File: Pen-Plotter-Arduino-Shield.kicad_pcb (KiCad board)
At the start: 2 copper layers, 68.6 x 53.3 mm, 41 parts, among them J1 CONN_08LOCK, J10 CONN_08LOCK, J11 CONN_04LOCK, J12 CONN_03LOCK, J13 691137710002, J14 CONN_03LOCK, J15 CONN_03LOCK, J16 CONN_03LOCK, J17 CONN_03LOCK, J18 CONN_03X2FEMALE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

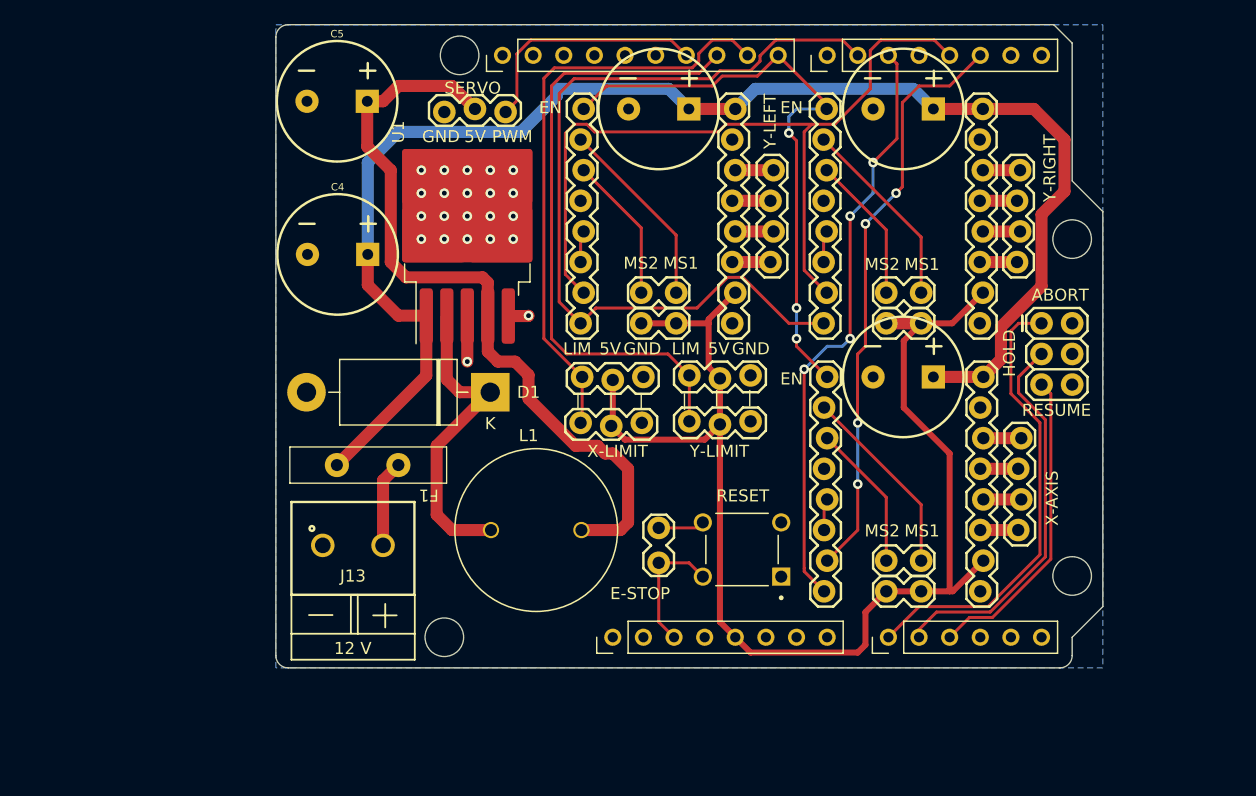
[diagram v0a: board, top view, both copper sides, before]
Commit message: update all files to Revision A
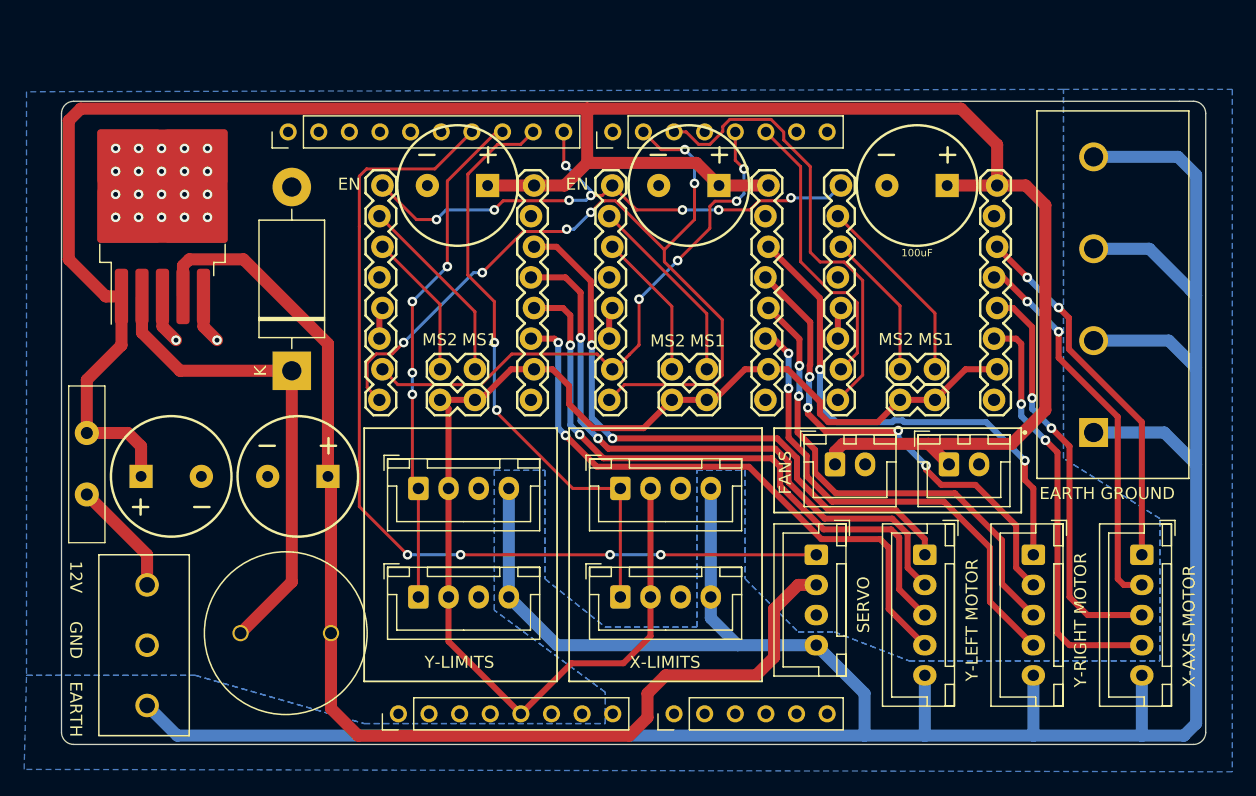
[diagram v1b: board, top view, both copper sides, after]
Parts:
- removed H1: MountingHole1, ArduinoMountingHoles:Arduino_MountingHole
- removed H2: MountingHole2, ArduinoMountingHoles:Arduino_MountingHole
- removed H3: MountingHole3, ArduinoMountingHoles:Arduino_MountingHole
- removed H4: MountingHole4, ArduinoMountingHoles:Arduino_MountingHole
- removed J13: 691137710002, FootPrints:691137710002
- removed S2: TS02-66-60-BK-160-LCR-D, FootPrints:SW_TS02-66-60-BK-160-LCR-D
- added J24: Conn_01x04, Connector_JST:JST_XH_B4B-XH-A_1x04_P2.50mm_Vertical, F.Cu at (151.5, 110.0)
- added J25: Conn_01x05, Connector_JST:JST_XH_B5B-XH-A_1x05_P2.50mm_Vertical, F.Cu at (178.5, 110.0)
- J11: value CONN_04LOCK -> Conn_01x02; footprint Connectors:1X04_LOCK -> Connector_JST:JST_XH_B2B-XH-A_1x02_P2.50mm_Vertical
- J12, J14, J15, J16: value CONN_03LOCK -> Conn_01x04; footprint Connectors:1X03_LOCK -> Connector_JST:JST_XH_B4B-XH-A_1x04_P2.50mm_Vertical
- J17: value CONN_03LOCK -> TB005_-762-04BE; footprint Connectors:1X03_LOCK -> FootPrints:CUI_TB005 -762-04BE
- J18: value CONN_03X2FEMALE -> 691137710003; footprint Connectors:2X3 -> FootPrints:691137710003
- J3: value CONN_02LOCK -> Conn_01x02; footprint Connectors:1X02_LOCK -> Connector_JST:JST_XH_B2B-XH-A_1x02_P2.50mm_Vertical
- J5, J8: value CONN_04LOCK -> Conn_01x05; footprint Connectors:1X04_LOCK -> Connector_JST:JST_XH_B5B-XH-A_1x05_P2.50mm_Vertical
- moved J18 78.8 mm to (96.0, 117.5)
- moved J12 41.5 mm to (135.2, 113.5), turned to 0 degrees
- moved J8 38.6 mm to (169.5, 110.0)
- moved J17 33.8 mm to (174.5, 99.9), turned to 90 degrees
- moved C5 31.3 mm to (108.5, 103.5)
- moved F1 30.1 mm to (84.0, 101.0), turned to 90 degrees
- moved U1 25.3 mm to (97.3, 80.9)
- moved J11 25.1 mm to (162.5, 102.5), turned to 0 degrees
- moved C4 23.0 mm to (98.0, 103.5), turned to 180 degrees
- moved L1 22.5 mm to (107.5, 116.5)
- moved J14 19.6 mm to (118.5, 113.5)
- moved U6 18.9 mm to (107.7, 74.9)
- moved C3 18.9 mm to (140.9, 79.4)
- moved J10 18.9 mm to (147.4, 97.2)
- moved J20 18.9 mm to (142.2, 94.6)
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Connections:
- J11 pad 1: /YR-1 -> /V_MOTOR
- J11 pad 2: /YR-2 -> GND
- J12 pad 1: /SERVO_PWM -> /X-LIMIT
- J12 pad 2: /SERVO_PWR -> 5V
- J14 pad 1: /X-LIMIT -> /Y-LIMIT
- J15 pad 1: /X-LIMIT -> /Y-LIMIT
- J16 pad 1: /Y-LIMIT -> /X-LIMIT
- J17 pad 1: /Y-LIMIT -> GNDPWR
- J17 pad 2: 5V -> GNDPWR
- J17 pad 3: GND -> GNDPWR
- J18 pad 1: /ABORT -> 12V
- J18 pad 3: /HOLD -> GNDPWR
- J3 pad 1: /RESET -> /V_MOTOR
- J3 pad 2: Net-(J3-Pad2) -> GND
- J5 pad 1: /X_1 -> /YL-1
- J5 pad 2: /X_2 -> /YL-2
- J5 pad 3: /X_3 -> /YL-3
- J5 pad 4: /X_4 -> /YL-4
- J8 pad 1: /YL-1 -> /YR-1
- J8 pad 2: /YL-2 -> /YR-2
- J8 pad 3: /YL-3 -> /YR-3
- J8 pad 4: /YL-4 -> /YR-4
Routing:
- net GNDPWR: track 0.00 -> 247.2 mm
- net /V_MOTOR: track 121.9 -> 196.7 mm
- net /SERVO_PWM: track 20.3 -> 77.8 mm, vias 0 -> 4
- net /YL-2: track 3.17 -> 52.1 mm, vias 0 -> 2
- net /YL-3: track 3.18 -> 51.7 mm, vias 0 -> 2
- net /YL-1: track 3.18 -> 51.3 mm, vias 0 -> 2
- net /YL-4: track 3.17 -> 50.3 mm, vias 0 -> 2
- net /YR-1: track 3.09 -> 42.1 mm, vias 0 -> 2
- net /ABORT: track 37.8 -> 0.00 mm
- net /YR-3: track 3.09 -> 40.5 mm, vias 0 -> 2
- net /YR-4: track 3.09 -> 40.5 mm, vias 0 -> 2
- net /YR-2: track 3.09 -> 40.2 mm, vias 0 -> 4
- net /SERVO_PWR: track 64.3 -> 97.9 mm
- net /X_4: track 2.92 -> 35.1 mm, vias 0 -> 2
- net /HOLD: track 32.2 -> 0.00 mm
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- added copper zone on B.Cu, net GNDPWR
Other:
- board size 68.6 x 53.3 mm -> 94.9 x 53.3 mm
- rule pad_to_mask_clearance: 0 -> 0.0508
- board text added: "12V"
- board text added: "EARTH"
- board text added: "EARTH GROUND"
- board text added: "FANS"
- board text added: "Pen Plotter Arduino Shield Rev A"
- board text added: "X-AXIS MOTOR"
- board text added: "X-LIMITS"
- board text added: "Y-LEFT MOTOR"
- board text added: "Y-LIMITS"
- board text added: "Y-RIGHT MOTOR"
- board text removed: "12 V"
- board text removed: "5V"
- board text removed: "ABORT"
- board text removed: "E-STOP"
- board text removed: "HOLD"
- board text removed: "LIM"
- board text removed: "PWM"
- board text removed: "Pen Plotter Arduino Shield Rev -"
- board text removed: "RESET"
- board text removed: "RESUME"
- board text removed: "X-AXIS"
- board text removed: "X-LIMIT"
- board text removed: "Y-LEFT"
- board text removed: "Y-LIMIT"
- board text removed: "Y-RIGHT"
- board text removed: "|"
